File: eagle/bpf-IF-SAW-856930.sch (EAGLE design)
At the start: 3 parts, among them U1 Qorvo 856930, X1 SMA-142-0701-801/806, X2 SMA-142-0701-801/806

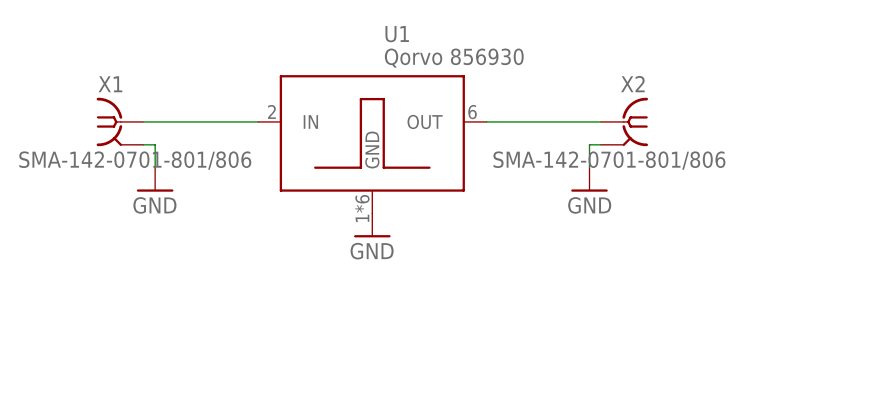
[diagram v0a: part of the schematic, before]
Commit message: Add IF-SAW-856930 layout
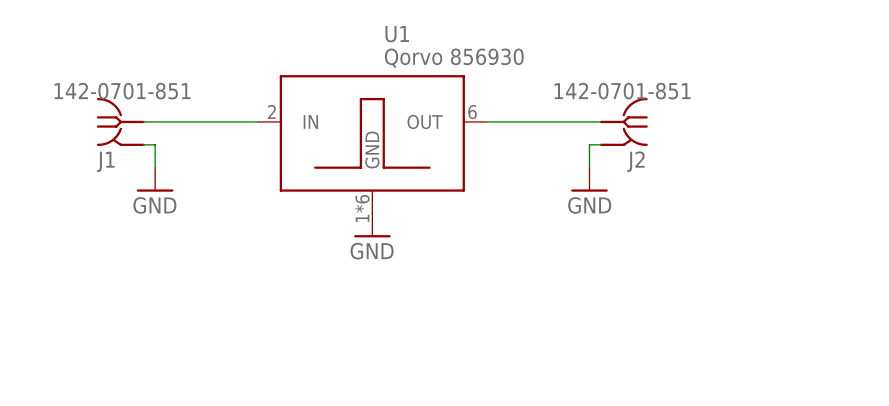
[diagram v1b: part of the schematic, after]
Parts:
- removed X1, X2: SMA-142-0701-801/806, con-coax:SMA-142-0701-801/806
- added J1, J2: 142-0701-851, J-Cinch-142-0701-851-SMA-end-launch:142-0701-851
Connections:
- net GND: now also J1.GND, J2.GND; no longer X1.2, X2.2
- net N$86: now also J1.RF; no longer X1.1
- net N$87: now also J2.RF; no longer X2.1
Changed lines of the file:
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@@
 <class number="0" name="default" width="0" drill="0">
+</class>
+<class number="1" name="RF" width="0" drill="0">
+<clearance class="1" value="0.6"/>
 </class>
 </classes>
 <parts>
 <part name="FRAME2" library="frames" library_urn="urn:adsk.eagle:library:229" deviceset="FRAME_A_L" device=""/>
-<part name="X1" library="con-coax" library_urn="urn:adsk.eagle:library:133" deviceset="SMA-" device="142-0701-801/806" package3d_urn="urn:adsk.eagle:package:6214/1"/>
 <part name="GND79" library="supply1" library_urn="urn:adsk.eagle:library:371" deviceset="GND" device=""/>
-<part name="X2" library="con-coax" library_urn="urn:adsk.eagle:library:133" deviceset="SMA-" device="142-0701-801/806" package3d_urn="urn:adsk.eagle:package:6214/1"/>
 <part name="GND91" library="supply1" library_urn="urn:adsk.eagle:library:371" deviceset="GND" device=""/>
 <part name="GND96" library="supply1" library_urn="urn:adsk.eagle:library:371" deviceset="GND" device=""/>
 <part name="U1" library="U-Qorvo-856930-SAW" deviceset="856930" device="" value="Qorvo 856930"/>
+<part name="J1" library="J-Cinch-142-0701-851-SMA-end-launch" deviceset="142-0701-851" device=""/>
+<part name="J2" library="J-Cinch-142-0701-851-SMA-end-launch" deviceset="142-0701-851" device=""/>
 </parts>
 <sheets>
@@
 <attribute name="DRAWING_NAME" x="190.5" y="19.05" size="2.54" layer="94"/>
 </instance>
-<instance part="X1" gate="G1" x="111.76" y="119.38" smashed="yes">
-<attribute name="VALUE" x="100.33" y="114.3" size="1.778" layer="96"/>
-<attribute name="NAME" x="109.22" y="122.682" size="1.778" layer="95"/>
-</instance>
 <instance part="GND79" gate="1" x="115.57" y="111.76" smashed="yes">
 <attribute name="VALUE" x="113.03" y="109.22" size="1.778" layer="96"/>
-</instance>
-<instance part="X2" gate="G1" x="167.64" y="119.38" smashed="yes" rot="MR0">
-<attribute name="VALUE" x="179.07" y="114.3" size="1.778" layer="96" rot="MR0"/>
-<attribute name="NAME" x="170.18" y="122.682" size="1.778" layer="95" rot="MR0"/>
 </instance>
 <instance part="GND91" gate="1" x="163.83" y="111.76" smashed="yes" rot="MR0">
@@
 <attribute name="VALUE" x="140.97" y="125.73" size="1.778" layer="96"/>
 </instance>
+<instance part="J1" gate="G$1" x="111.76" y="119.38" smashed="yes">
+<attribute name="NAME" x="109.22" y="114.3" size="1.778" layer="95"/>
+<attribute name="VALUE" x="104.14" y="121.92" size="1.778" layer="96"/>
+</instance>
+<instance part="J2" gate="G$1" x="167.64" y="119.38" smashed="yes" rot="MR0">
+<attribute name="NAME" x="170.18" y="114.3" size="1.778" layer="95" rot="MR0"/>
+<attribute name="VALUE" x="175.26" y="121.92" size="1.778" layer="96" rot="MR0"/>
+</instance>
 </instances>
 <busses>
@@
 <net name="GND" class="0">
 <segment>
-<pinref part="X1" gate="G1" pin="2"/>
 <pinref part="GND79" gate="1" pin="GND"/>
 <wire x1="114.3" y1="116.84" x2="115.57" y2="116.84" width="0.1524" layer="91"/>
 <wire x1="115.57" y1="116.84" x2="115.57" y2="114.3" width="0.1524" layer="91"/>
+<pinref part="J1" gate="G$1" pin="GND"/>
 </segment>
 <segment>
-<pinref part="X2" gate="G1" pin="2"/>
 <pinref part="GND91" gate="1" pin="GND"/>
 <wire x1="165.1" y1="116.84" x2="163.83" y2="116.84" width="0.1524" layer="91"/>
 <wire x1="163.83" y1="116.84" x2="163.83" y2="114.3" width="0.1524" layer="91"/>
+<pinref part="J2" gate="G$1" pin="GND"/>
 </segment>
 <segment>
@@
 </segment>
 </net>
-<net name="N$86" class="0">
+<net name="N$86" class="1">
 <segment>
-<pinref part="X1" gate="G1" pin="1"/>
 <wire x1="114.3" y1="119.38" x2="127" y2="119.38" width="0.1524" layer="91"/>
 <pinref part="U1" gate="G$1" pin="IN"/>
+<pinref part="J1" gate="G$1" pin="RF"/>
 </segment>
 </net>
-<net name="N$87" class="0">
+<net name="N$87" class="1">
 <segment>
-<pinref part="X2" gate="G1" pin="1"/>
 <wire x1="165.1" y1="119.38" x2="152.4" y2="119.38" width="0.1524" layer="91"/>
 <pinref part="U1" gate="G$1" pin="OUT"/>
+<pinref part="J2" gate="G$1" pin="RF"/>
 </segment>
 </net>
@@
 will not be understood (or retained) with this version.
 </note>
-<note version="8.3" severity="warning">
-Since Version 8.3, EAGLE supports the association of 3D packages
-with devices in libraries, schematics, and board files. Those 3D
-packages will not be understood (or retained) with this version.
-</note>
 </compatibility>
